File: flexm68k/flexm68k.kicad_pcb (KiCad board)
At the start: 2 copper layers, 25 x 88 mm, 7 parts, among them J1 FPC-FFC-64, U1 MC68000

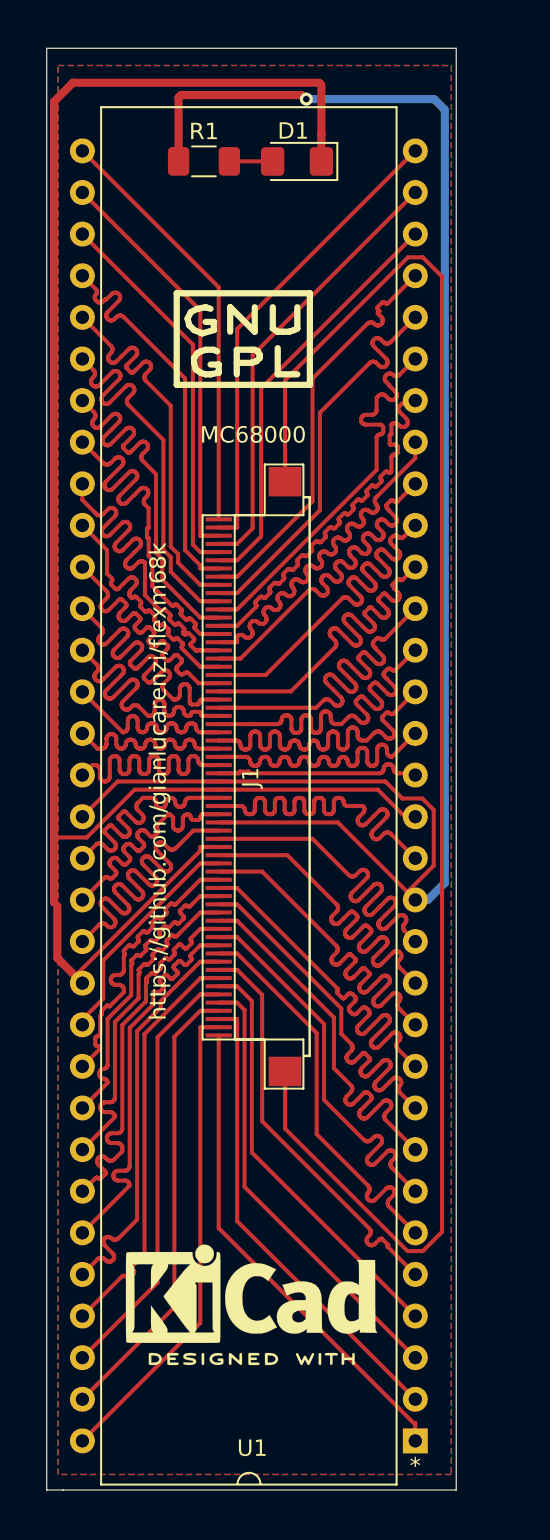
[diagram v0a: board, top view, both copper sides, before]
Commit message: Added LOGOs in the schematics, so the PCB will have them already. Run DRC for errors. Report only three (3) overlap for silkscreen and filled zones. No problem at all.
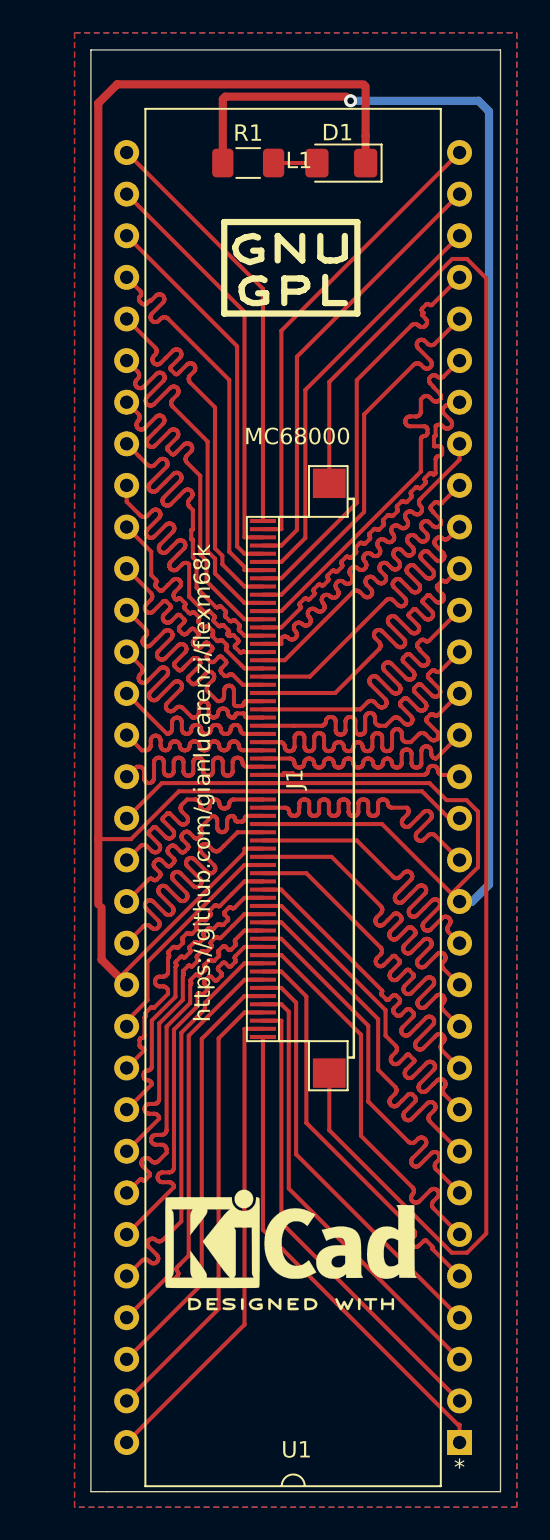
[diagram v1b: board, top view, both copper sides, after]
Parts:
- removed G***: LOGO, RetroBitLab:amigaLogo_BW_31x12mm
- removed GNULOGO: Symbol_GNU-GPL_CopperTop_Small, RetroBitLab:Symbol_GNU-GPL_SilkScreen_Small
- removed KICADLOGO: KiCad-Logo2_6mm_SilkScreen, Symbol:KiCad-Logo2_6mm_SilkScreen
- added L1: GNU GPL LOGO, RetroBitLab:Symbol_GNU-GPL_SilkScreen_Small, F.Cu at (151.2, 73.6)
- added L2: AMIGA LOGO, RetroBitLab:amigaLogo_BW_31x12mm, B.Cu at (150.2, 105.1)
- added L3: KiCad Logo, Symbol:KiCad-Logo2_6mm_SilkScreen, F.Cu at (151.2, 132.6)
- moved U1 2.70 mm to (161.5, 145.1)
- moved R1 2.70 mm to (148.6, 67.0)
- moved D1 2.70 mm to (154.3, 67.0)
- moved J1 2.70 mm to (149.5, 104.5)

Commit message: Wrong footprint for CPU. Now should be corrected
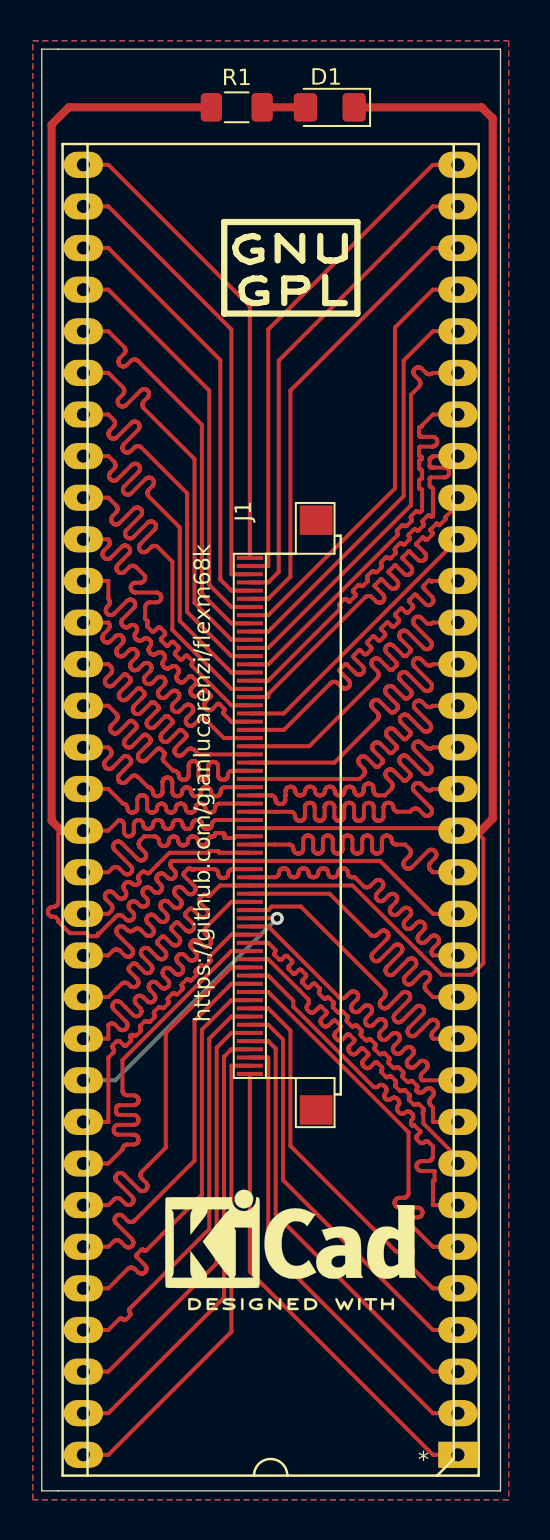
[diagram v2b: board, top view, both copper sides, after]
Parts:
- U1: footprint RetroBitLab:MC68000_REPLACEMENT -> RetroBitLab:DIP-64_W22.86mm_Socket_LongPads_Socket
- moved R1 3.47 mm to (147.9, 63.5)
- moved D1 3.47 mm to (153.6, 63.6)
- moved J1 2.39 mm to (148.7, 106.8)
- moved U1 0.76 mm to (161.4, 145.8)
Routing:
- net Net-(J1-Pad0): track 94.3 -> 0.00 mm
- net /P33: track 12.8 -> 24.9 mm
- net /P22: track 14.0 -> 25.0 mm
- net /P38: track 12.7 -> 22.8 mm
- net /P46: track 15.9 -> 25.1 mm
- net /P45: track 25.0 -> 17.1 mm
- net /P36: track 12.5 -> 18.8 mm
- net /P35: track 19.3 -> 25.1 mm
- net /P40: track 19.7 -> 25.0 mm
- net /P44: track 18.7 -> 23.3 mm
- net VCC: track 112.7 -> 108.3 mm, vias 1 -> 0
- net /P16: track 20.7 -> 25.0 mm
- net /P64: track 25.9 -> 29.1 mm
- net /P62: track 25.1 -> 28.2 mm
- net /P60: track 23.5 -> 26.7 mm
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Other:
- board size 25 x 88 mm -> 28 x 88 mm

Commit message: Modified for correct footprint CPU
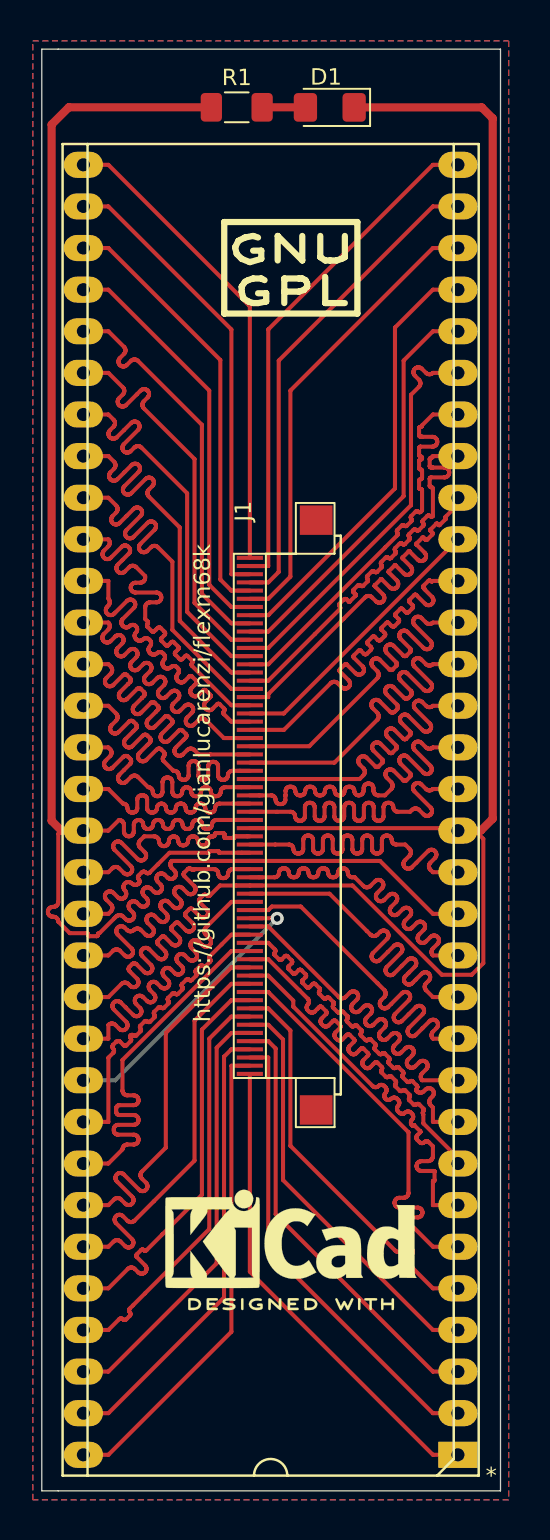
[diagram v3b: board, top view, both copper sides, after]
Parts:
- U1: footprint RetroBitLab:DIP-64_W22.86mm_Socket_LongPads_Socket -> RetroBitLab:MC68000-RELOCATOR-MALE
